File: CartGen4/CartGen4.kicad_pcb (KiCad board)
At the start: 4 copper layers, 52.8 x 60.9 mm, 77 parts, among them J1 MEM2080-00-128-00-A, SW1 SW_Push, U1 TPS65266-1RHBR, U10 IS25WP080D-JNLE, U11 DS1391U-33+, U2 SN74LV1T34DCKR, U3 SIT8008BI-73-33E-33.333333G, U4 NXS0108BQX, U5 AS1C8M16PL-70BIN, U6 NXS0108BQX, U7 NXS0108BQX, U8 NXS0104BQX, U9 LFXP2-8E-5MN132C, Y1 FC-135R 32.7680KA-E5

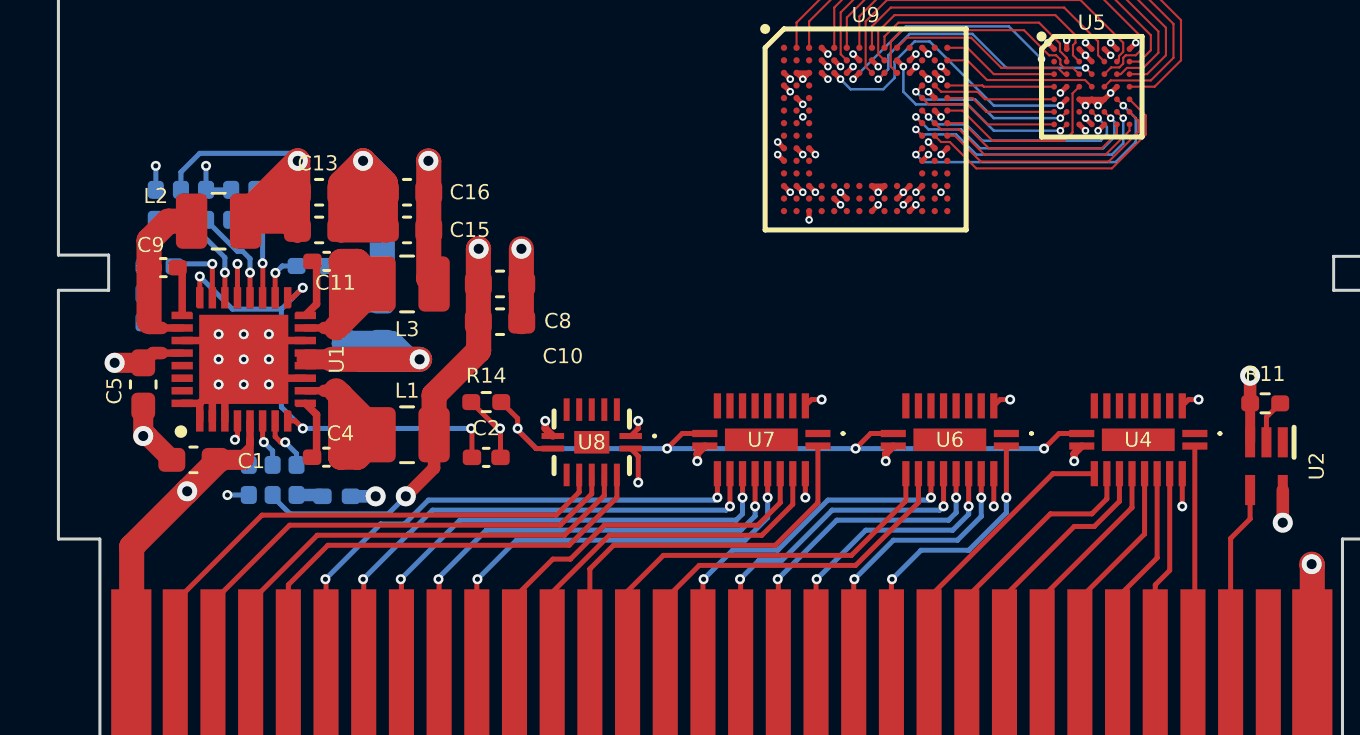
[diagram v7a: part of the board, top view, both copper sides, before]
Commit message: Connected bus transceivers
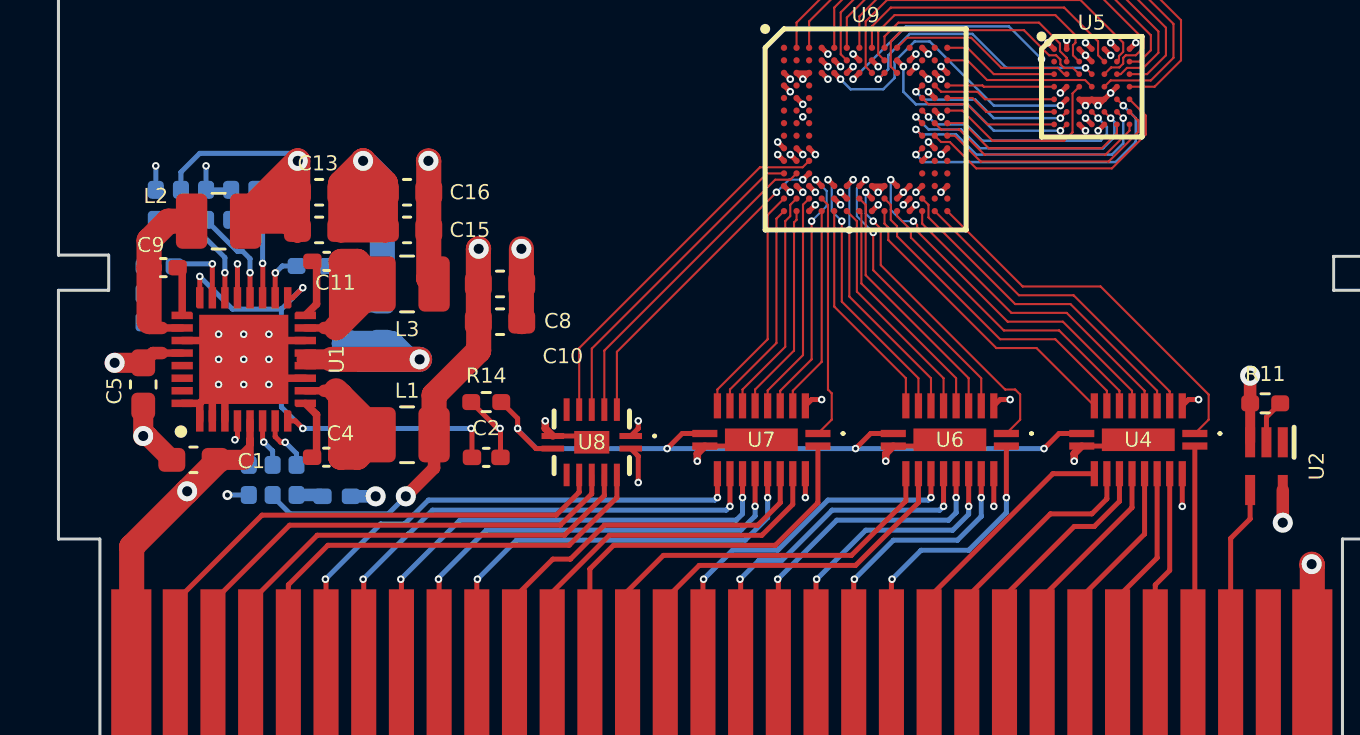
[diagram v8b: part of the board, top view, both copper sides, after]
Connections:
- U9 pad M7: GB_ADDR12 -> GB_ADDR14
- U9 pad N12: GB_DATA6 -> GB_DATA5
- U9 pad P13: GB_DATA5 -> GB_DATA6
- U9 pad P7: GB_ADDR14 -> GB_ADDR12
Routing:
- net GB_DATA7: track 0.00 -> 15.2 mm
- net GB_DATA3: track 0.00 -> 14.9 mm, vias 0 -> 2
- net GB_CLK: track 0.00 -> 14.7 mm
- net GB_DATA5: track 0.00 -> 13.4 mm
- net GB_DATA1: track 0.00 -> 13.2 mm
- net GB_WR#: track 0.00 -> 13.0 mm
- net GB_ADDR15: track 0.00 -> 13.0 mm, vias 0 -> 2
- net GB_RD#: track 0.00 -> 12.9 mm
- net GB_DATA6: track 0.00 -> 12.9 mm
- net GB_CS#: track 0.00 -> 12.9 mm, vias 0 -> 2
- net GB_DATA4: track 0.00 -> 12.7 mm
- net GB_DATA2: track 0.00 -> 12.7 mm
- net GB_DATA0: track 0.00 -> 12.1 mm
- net GB_ADDR14: track 0.00 -> 11.5 mm, vias 0 -> 2
- net GB_ADDR9: track 0.00 -> 10.8 mm, vias 0 -> 2
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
